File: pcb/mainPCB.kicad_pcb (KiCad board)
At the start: 4 copper layers, 160 x 73.2 mm, 161 parts, among them IC1 FXL6408UMX, IC2 ATA6561-GAQW-N, IC3 ICL3221EIVZ, J1 PTSM-Header-Horizontal-6, J10 Conn_01x08_Female, J11 Conn_01x08_Female, J12 Conn_02x02_Odd_Even, J13 SM04B-SRSS-TB(LF)(SN), J14 USB_B_Micro, J15 RJ45_Amphenol_RJMG1BD3B8K1ANR, J16 DB9_Male_MountingHoles, J17 SM04B-SRSS-TB(LF)(SN), J18 PTSM-Header-Horizontal-2, J3 PTSM-Header-Horizontal-7, J4 CCA-Header-Horizontal-4, J5 PTSM-Header-Horizontal-5, J7 Conn_01x04_Male, J8 Conn_01x04_Male, J9 Conn_01x08_Female, K1 CP1SA-12V-Z, K2 CP1SA-12V-Z, Q1 BC817-40,215, Q2 BC817-40,215, SW1 SW_Push, U1 ESP32-WROOM-32, U10 NUD3124LT1G, U11 LAN8720A, U12 LSM9DS1, U2 AZ1117-3.3, U3 VNH7070AS, U4 ADS1115IDGS, U5 VNH7070AS, U6 PCA9306DCTR, U7 TPD3E001DRLR, U8 CP2102N-A01-GQFN24, U9 VNH7070AS

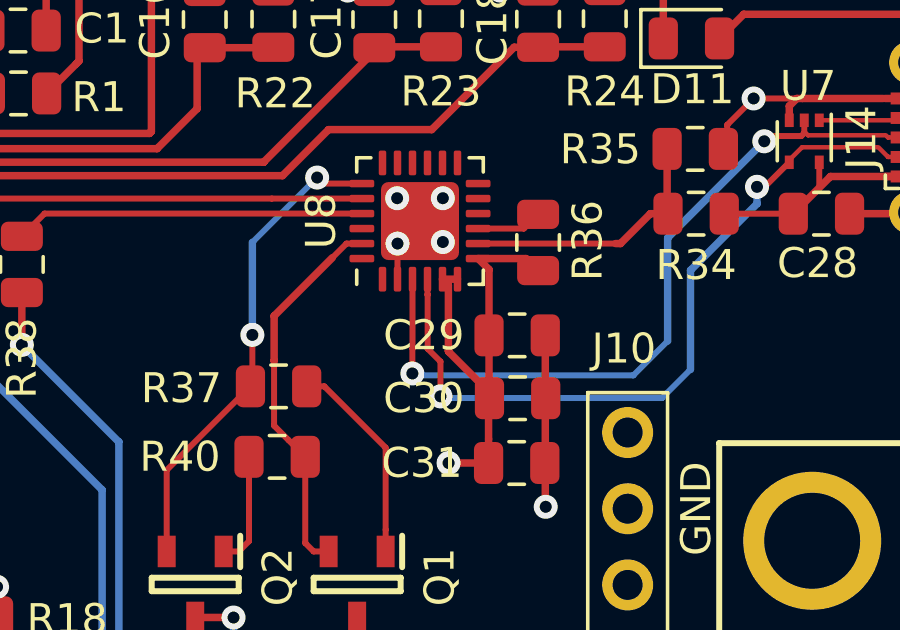
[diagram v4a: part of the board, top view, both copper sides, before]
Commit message: Removed 'internal soldering bridges' for easier inspection
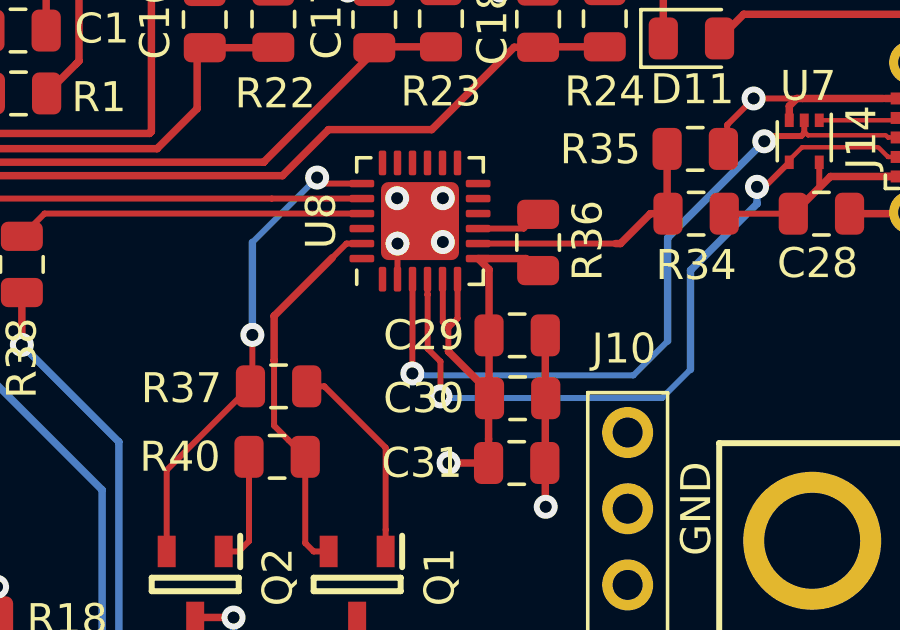
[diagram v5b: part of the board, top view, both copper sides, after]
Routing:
- net +3V3: track 84.0 -> 85.3 mm
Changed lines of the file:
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@@
     (thickness 1.6)
     (drawings 55)
-    (tracks 1827)
+    (tracks 1831)
     (zones 0)
     (modules 161)
@@
   (segment (start 158.8285 60.3885) (end 158.8285 58.192) (width 0.25) (layer F.Cu) (net 5))
   (segment (start 158.8135 62.514) (end 158.8435 62.484) (width 0.25) (layer F.Cu) (net 5))
-  (segment (start 157.7775 58.516) (end 157.2775 58.516) (width 0.25) (layer F.Cu) (net 5))
-  (segment (start 157.47321 58.71171) (end 157.47321 60.90329) (width 0.25) (layer F.Cu) (net 5))
-  (segment (start 157.2775 58.516) (end 157.47321 58.71171) (width 0.25) (layer F.Cu) (net 5))
   (segment (start 158.8135 63.843) (end 158.8135 64.643) (width 0.25) (layer F.Cu) (net 5))
   (segment (start 158.8135 62.263946) (end 158.8135 63.843) (width 0.25) (layer F.Cu) (net 5))
@@
   (via (at 67.83832 107.666) (size 0.8) (drill 0.4) (layers F.Cu B.Cu) (net 1))
   (segment (start 75.819 107.666) (end 67.83832 107.666) (width 0.25) (layer F.Cu) (net 1))
+  (segment (start 157.28696 58.52546) (end 157.2775 58.516) (width 0.2) (layer F.Cu) (net 5))
+  (segment (start 157.28696 59.94742) (end 157.28696 58.52546) (width 0.2) (layer F.Cu) (net 5))
+  (segment (start 157.47321 60.13367) (end 157.28696 59.94742) (width 0.2) (layer F.Cu) (net 5))
+  (segment (start 157.77972 59.82716) (end 157.47321 60.13367) (width 0.2) (layer F.Cu) (net 5))
+  (segment (start 157.7775 58.516) (end 157.77972 58.51822) (width 0.2) (layer F.Cu) (net 5))
+  (segment (start 157.77972 58.51822) (end 157.77972 59.82716) (width 0.2) (layer F.Cu) (net 5))
+  (segment (start 157.47321 60.90329) (end 157.47321 60.13367) (width 0.2) (layer F.Cu) (net 5))
   (via (at 131.33832 43.19016) (size 0.8) (drill 0.4) (layers F.Cu B.Cu) (net 9))
   (segment (start 131.343999 43.195839) (end 131.33832 43.19016) (width 0.25) (layer F.Cu) (net 9))

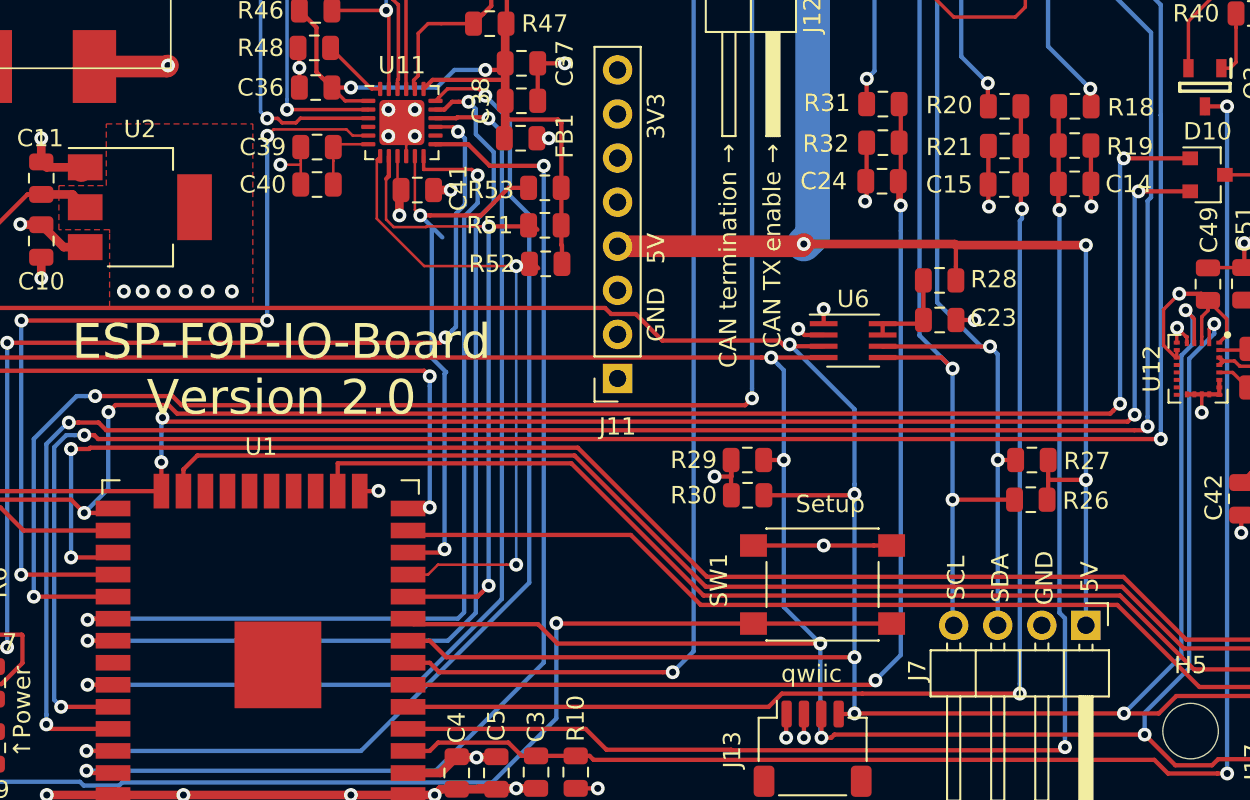
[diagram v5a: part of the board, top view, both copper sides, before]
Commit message: Minor cosmetic changes on tracks
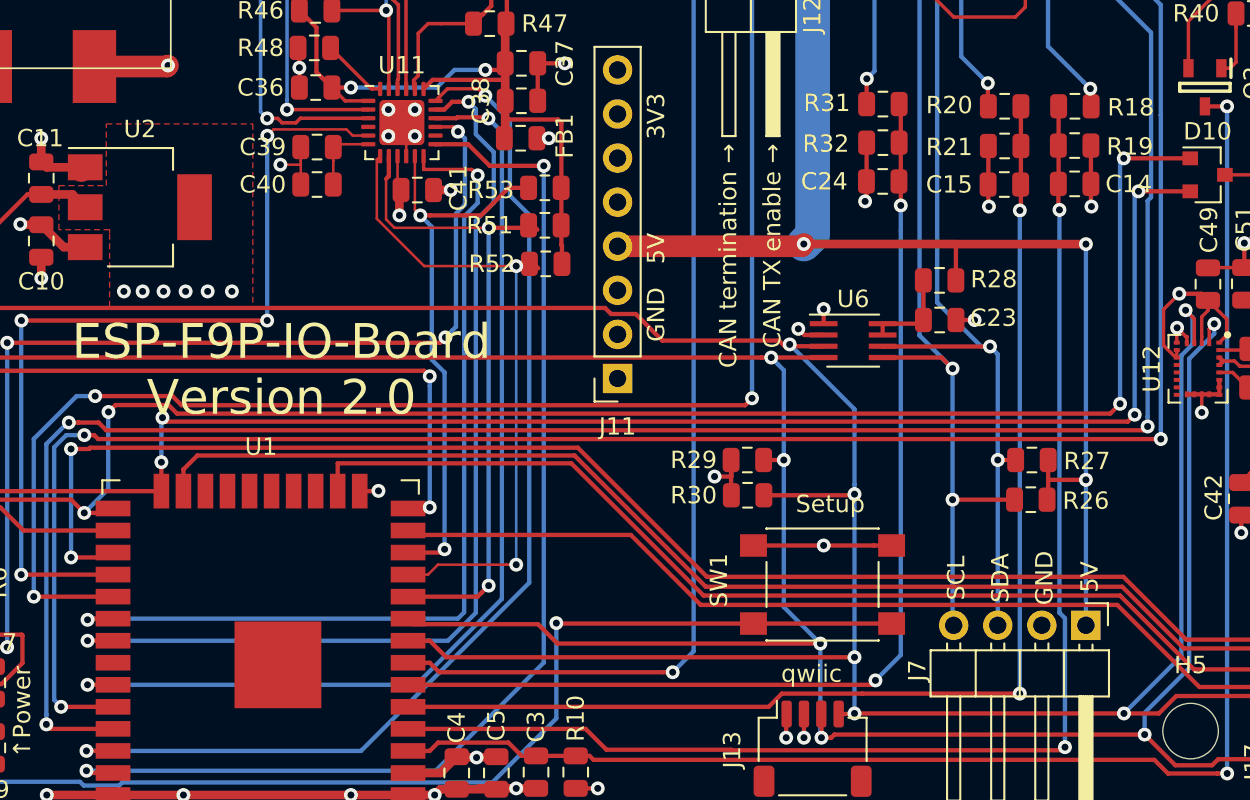
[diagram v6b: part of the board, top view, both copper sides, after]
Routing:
- net /Input_3/output: track 62.3 -> 60.9 mm
- net /LAN8720/EMAC_RX_CRS_DV:GPIO27: track 33.6 -> 32.7 mm

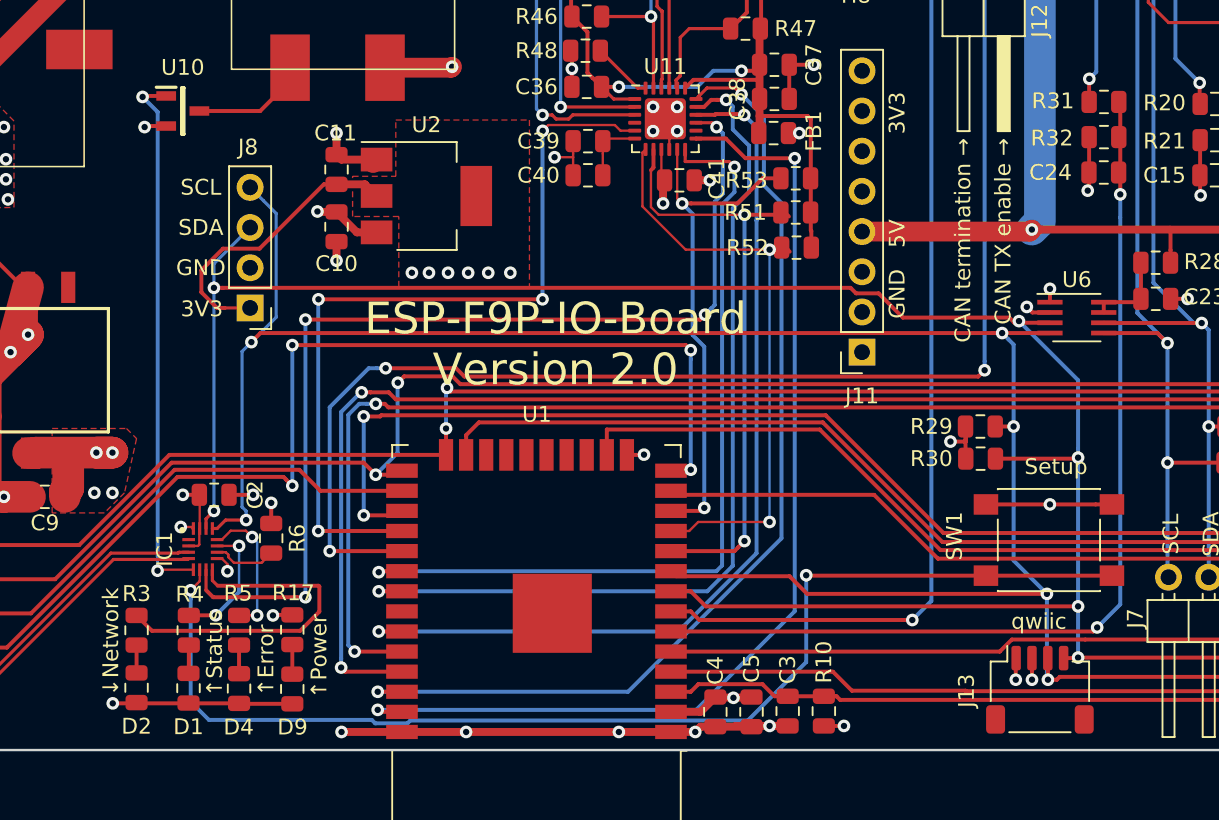
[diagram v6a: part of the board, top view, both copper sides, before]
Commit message: Moved Setup button switch. fixes #7
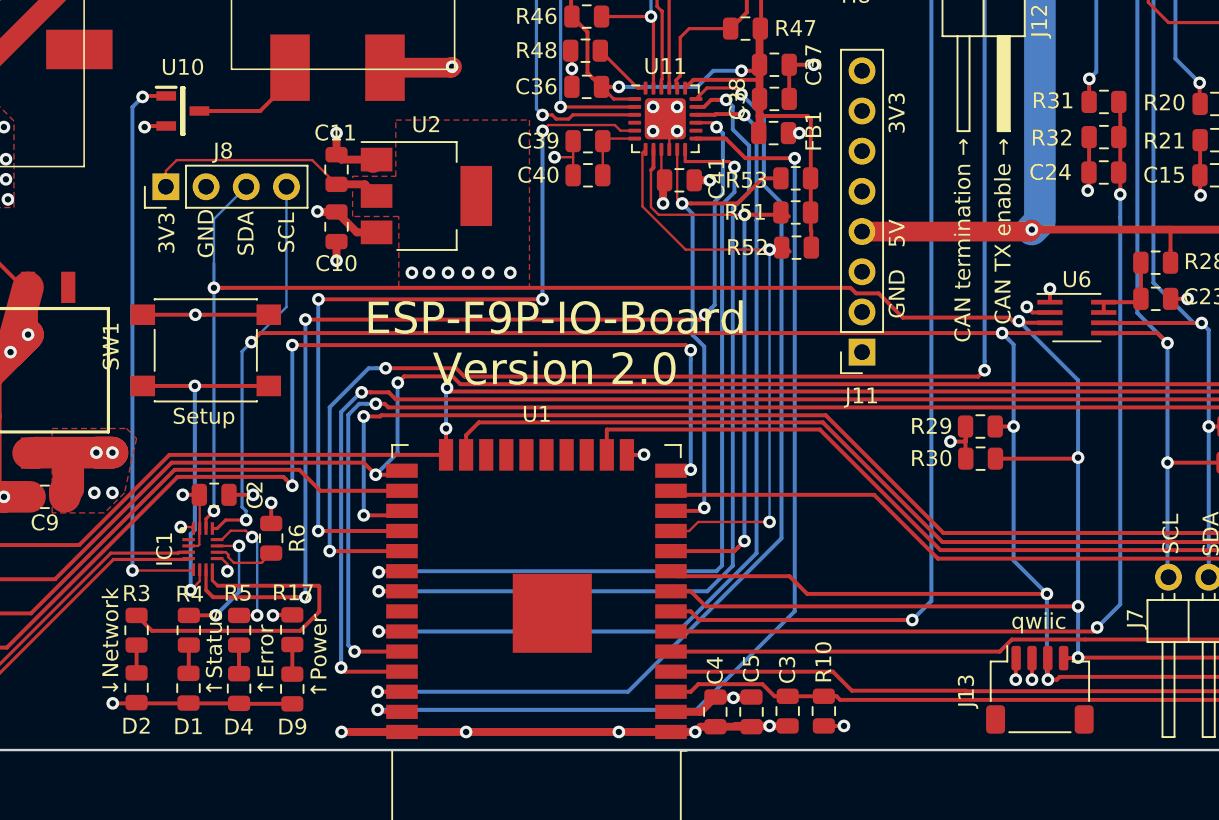
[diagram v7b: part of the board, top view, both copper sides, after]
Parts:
- moved SW1 54.6 mm to (73.7, 85.4)
- moved J8 9.33 mm to (71.2, 75.0), turned to 90 degrees
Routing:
- net Net-(IC1-Pad6): track 74.5 -> 22.5 mm
- net +3V3: track 85.3 -> 82.2 mm
- net /I2C_3_SDA: track 186.7 -> 189.2 mm
- net /Relais/Enable: track 34.1 -> 35.6 mm
